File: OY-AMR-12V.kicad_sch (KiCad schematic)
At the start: 21 parts

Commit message: Upgraded to Kicad 9
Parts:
- D?: value SA16CA -> SA16CA

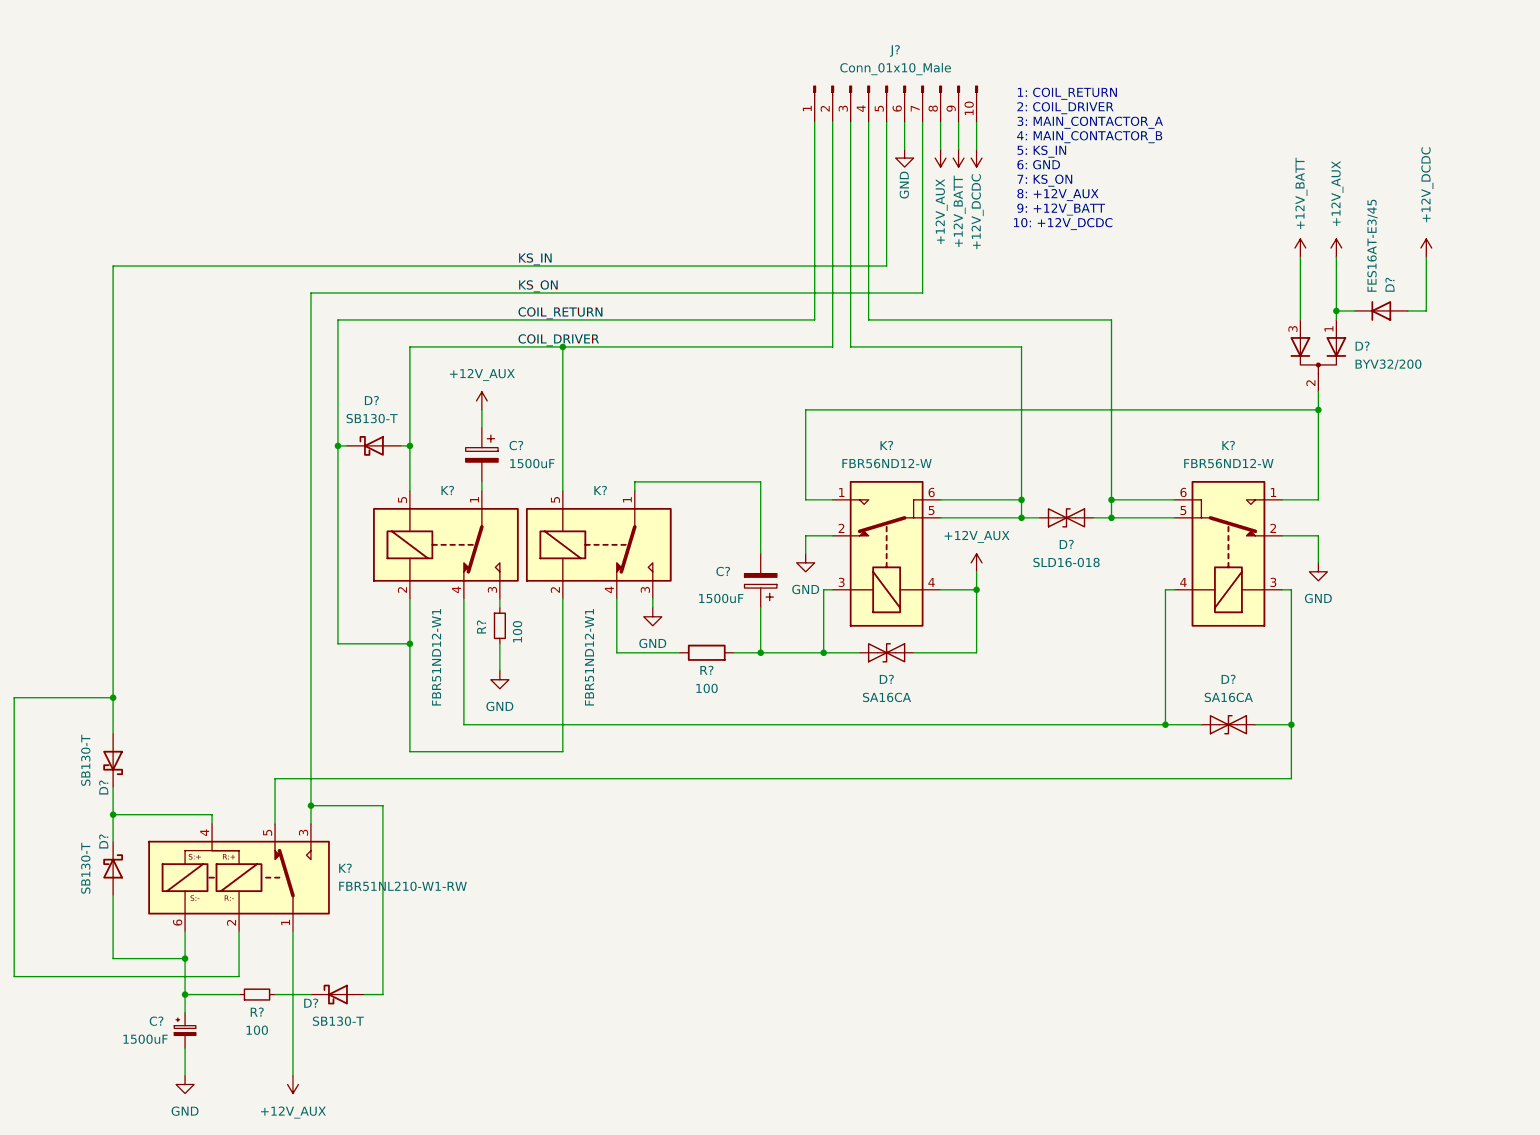
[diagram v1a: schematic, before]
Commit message: Annotated and added footprints
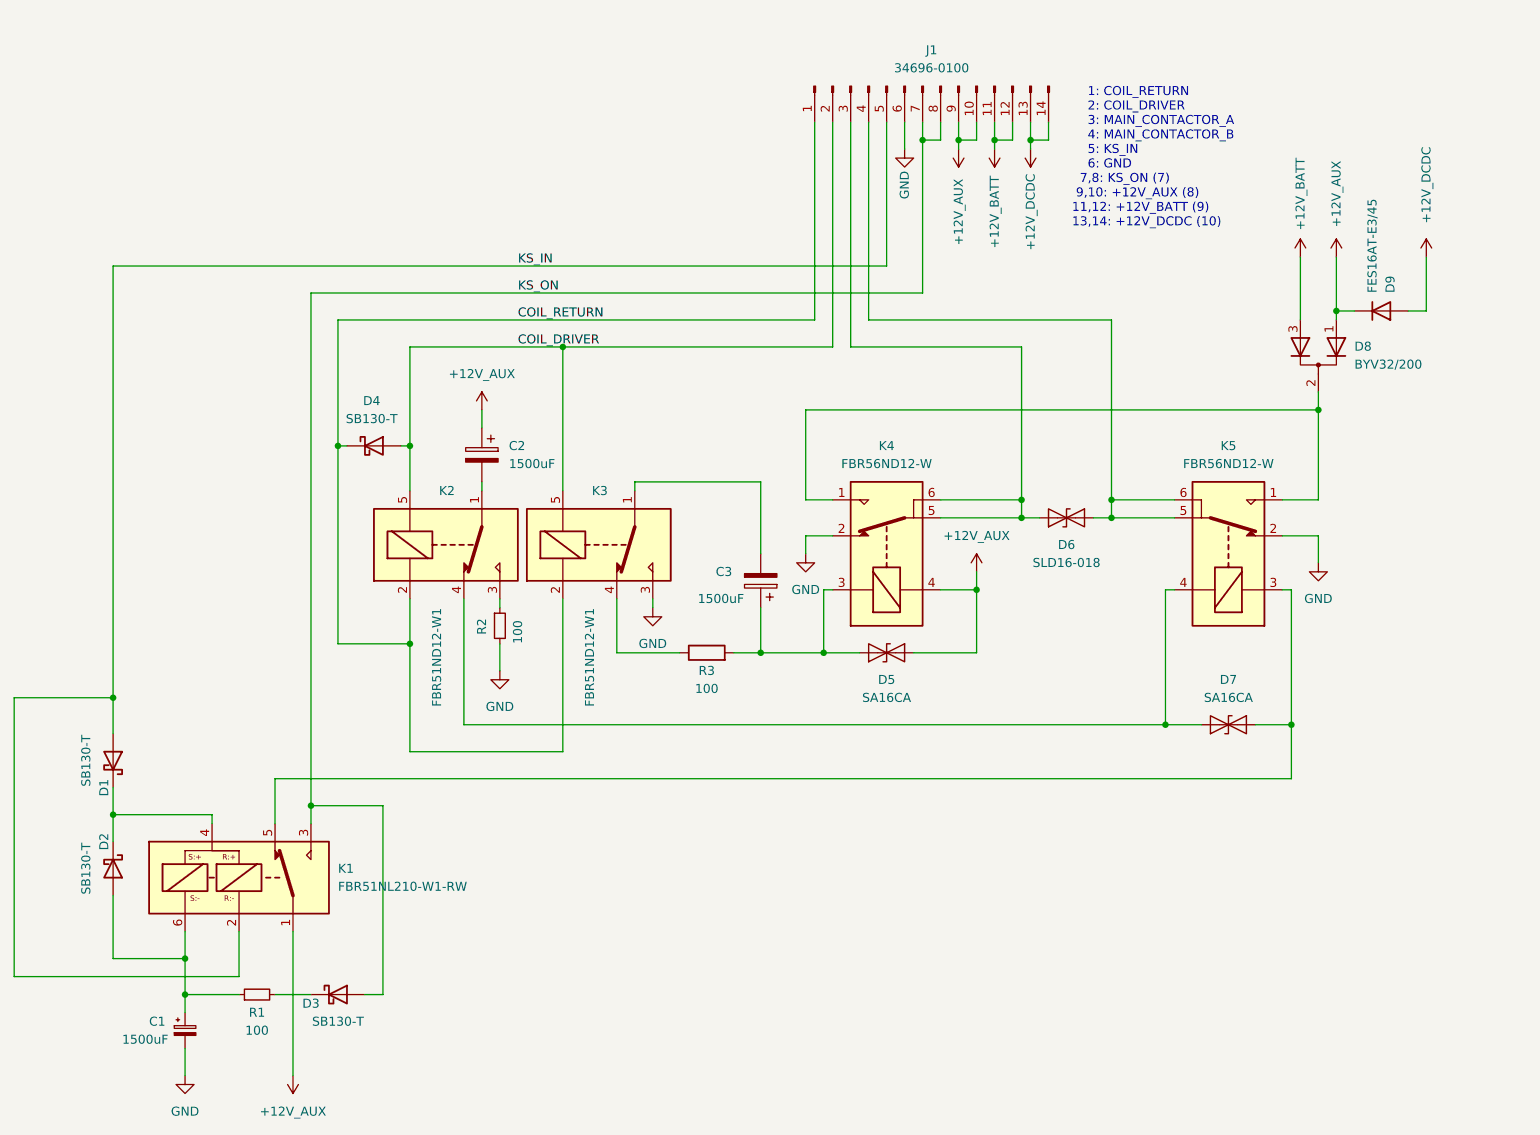
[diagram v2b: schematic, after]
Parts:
- removed J?: Conn_01x10_Male, symbol Connector:Conn_01x10_Male
- added J1: 34696-0100, SamacSys_Parts:0346960100, symbol Connector:Conn_01x14_Pin
- C1, C2, C3: renamed from C?; footprint (none) -> Capacitor_THT:CP_Radial_D16.0mm_P7.50mm
- D1, D2, D3, D4: renamed from D?; footprint (none) -> Diode_THT:D_DO-41_SOD81_P10.16mm_Horizontal
- D5, D7: renamed from D?; footprint Diode_SMD:D_SOD-323 -> Diode_THT:D_T-1_P10.16mm_Horizontal
- D6: renamed from D?; footprint (none) -> Diode_THT:D_P600_R-6_P20.00mm_Horizontal
- D8: renamed from D?; footprint (none) -> Package_TO_SOT_THT:TO-220-3_Vertical
- D9: renamed from D?; footprint (none) -> Package_TO_SOT_THT:TO-220-2_Vertical
- K1: renamed from K?; footprint (none) -> SamacSys_Parts:FBR51NL210W1RW
- K2, K3: renamed from K?; footprint Relay_THT:Relay_SPDT_Omron_G6E -> SamacSys_Parts:FBR51ND12-W1
- K4, K5: renamed from K?; footprint Relay_THT:Relay_SPDT_Omron_G6E -> SamacSys_Parts:FBR56ND12W
- R1, R2, R3: renamed from R?; footprint (none) -> Resistor_THT:R_Axial_DIN0207_L6.3mm_D2.5mm_P10.16mm_Horizontal
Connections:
- net +12V_AUX: now also J1.10 (Pin_10), J1.9 (Pin_9)
- net +12V_BATT: now also J1.11 (Pin_11), J1.12 (Pin_12)
- net +12V_DCDC: now also J1.13 (Pin_13), J1.14 (Pin_14)
- net COIL_DRIVER: now also J1.2 (Pin_2)
- net COIL_RETURN: now also J1.1 (Pin_1)
- net GND: now also J1.6 (Pin_6)
- net KS_IN: now also J1.5 (Pin_5)
- net KS_ON: now also J1.7 (Pin_7), J1.8 (Pin_8)
- net at D6.1 (A1), K4.5, K4.6: now also J1.3 (Pin_3)
- net at D6.2 (A2), K5.5, K5.6: now also J1.4 (Pin_4)
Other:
- note added: "1: COIL_RETURN 2: COIL_DRIVER 3: MAIN_CONTACTOR_A 4: MAIN_CONTACTOR_B 5: KS_IN 6: GND 7,8: KS_ON (7) 9,10: +12V_AUX (8) 11,12: +12V_BATT (9) 13,14: +12V_DCDC (10)"
- note removed: "1: COIL_RETURN 2: COIL_DRIVER 3: MAIN_CONTACTOR_A 4: MAIN_CONTACTOR_B 5: KS_IN 6: GND 7: KS_ON 8: +12V_AUX 9: +12V_BATT 10: +12V_DCDC"

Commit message: Initial PCB placements
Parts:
- D8: footprint Package_TO_SOT_THT:TO-220-3_Vertical -> Package_TO_SOT_THT:TO-220-3_Horizontal_TabDown
- D9: footprint Package_TO_SOT_THT:TO-220-2_Vertical -> Package_TO_SOT_THT:TO-220-2_Horizontal_TabDown
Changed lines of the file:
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@@
 			)
 		)
-		(property "Footprint" "Package_TO_SOT_THT:TO-220-2_Vertical"
+		(property "Footprint" "Package_TO_SOT_THT:TO-220-2_Horizontal_TabDown"
 			(at 240.03 62.23 0)
 			(effects
@@
 		(on_board yes)
 		(dnp no)
-		(fields_autoplaced yes)
 		(property "Reference" "D8"
-			(at 236.22 67.2464 90)
+			(at 222.504 66.294 90)
 			(effects
 				(font
@@
 		)
 		(property "Value" "BYV32/200"
-			(at 236.22 69.7864 90)
+			(at 215.646 68.834 90)
 			(effects
 				(font
@@
 			)
 		)
-		(property "Footprint" "Package_TO_SOT_THT:TO-220-3_Vertical"
+		(property "Footprint" "Package_TO_SOT_THT:TO-220-3_Horizontal_TabDown"
 			(at 231.14 69.85 0)
 			(effects

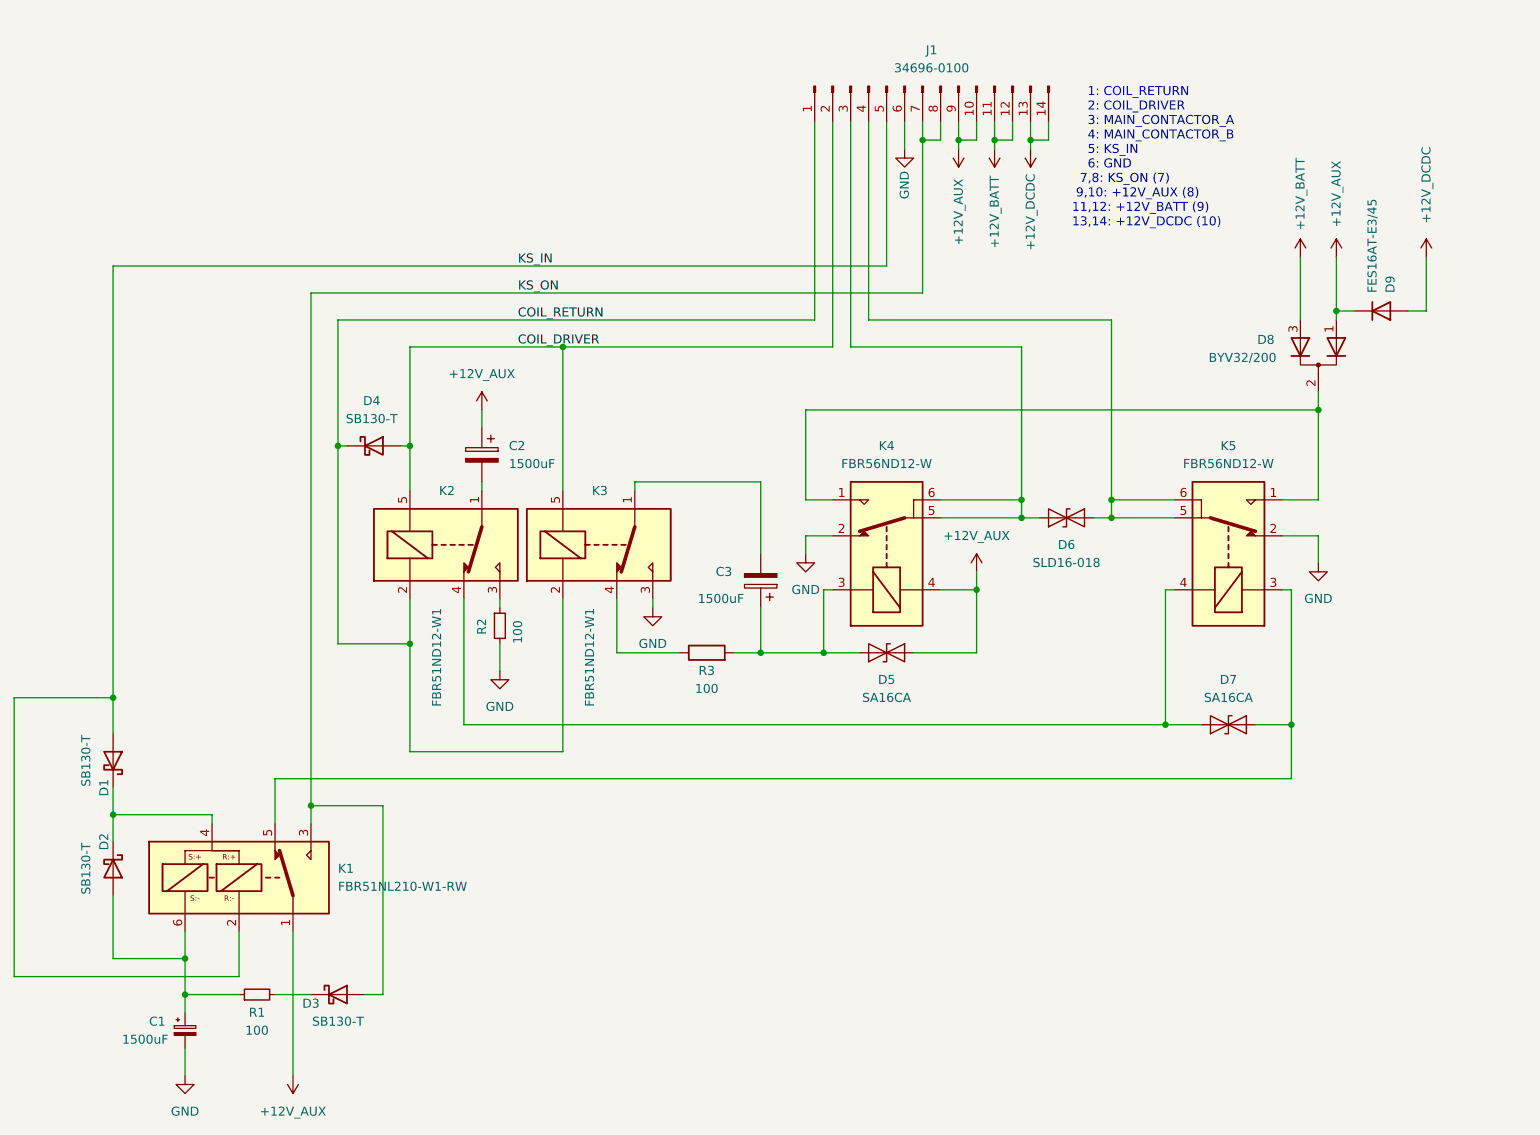
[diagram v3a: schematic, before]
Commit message: Added charge relay + precharge resistor for DC/DC
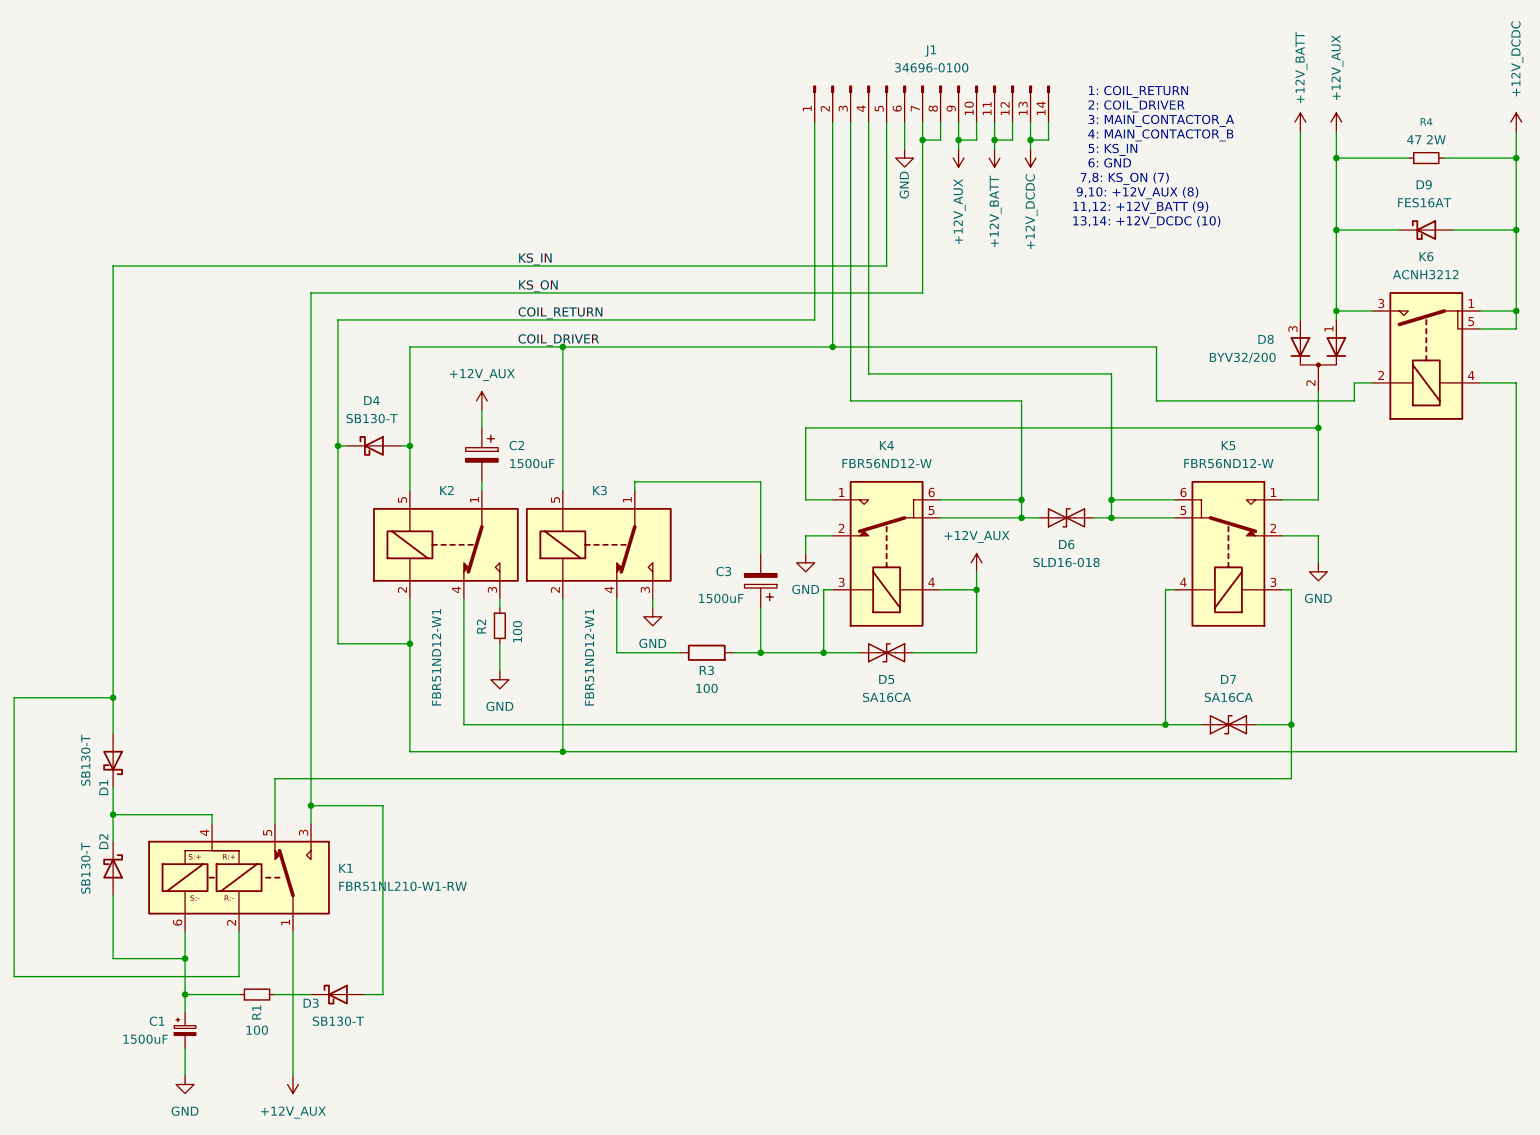
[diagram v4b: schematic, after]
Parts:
- removed D9: FES16AT-E3/45, Package_TO_SOT_THT:TO-220-2_Horizontal_TabDown, symbol Device:D
- added D9: FES16AT, Package_TO_SOT_THT:TO-220-2_Horizontal_TabDown, symbol Device:D_Schottky
- added K6: ACNH3212, SamacSys_Parts:ACNH3212, symbol Miscellaneous:ACNH3212
- added R4: 47 2W, Resistor_THT:R_Axial_DIN0411_L9.9mm_D3.6mm_P15.24mm_Horizontal, symbol Device:R_Small
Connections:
- net +12V_AUX: now also D9.1 (K), K6.3, R4.1
- net +12V_DCDC: now also D9.2 (A), K6.1, K6.5, R4.2
- net COIL_DRIVER: now also K6.2
- net COIL_RETURN: now also K6.4

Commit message: PCB layout in progress
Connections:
- net COIL_DRIVER: now also J1.6 (Pin_6); no longer J1.2 (Pin_2)
- net COIL_RETURN: now also J1.5 (Pin_5); no longer J1.1 (Pin_1)
- net GND: now also J1.2 (Pin_2); no longer J1.6 (Pin_6)
- net KS_IN: now also J1.1 (Pin_1); no longer J1.5 (Pin_5)
- net at D6.1 (A1), K4.5, K4.6: now also J1.4 (Pin_4); no longer J1.3 (Pin_3)
- net at D6.2 (A2), K5.5, K5.6: now also J1.3 (Pin_3); no longer J1.4 (Pin_4)
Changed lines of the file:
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@@
+	)
+	(junction
+		(at 172.72 67.31)
+		(diameter 0)
+		(color 0 0 0 0)
 	)
 	(junction
@@
 	)
 	(junction
-		(at 162.56 67.31)
-		(diameter 0)
-		(color 0 0 0 0)
-	)
-	(junction
 		(at 227.33 120.65)
 		(diameter 0)
@@
 	(wire
 		(pts
-			(xy 165.1 74.93) (xy 165.1 35.56)
-		)
-		(stroke
-			(width 0)
-			(type default)
-		)
-	)
-	(wire
-		(pts
 			(xy 161.29 110.49) (xy 152.4 110.49)
 		)
@@
 	(wire
 		(pts
+			(xy 167.64 35.56) (xy 167.64 74.93)
+		)
+		(stroke
+			(width 0)
+			(type default)
+		)
+	)
+	(wire
+		(pts
 			(xy 185.42 38.1) (xy 185.42 39.37)
 		)
@@
 	(wire
 		(pts
+			(xy 172.72 35.56) (xy 172.72 67.31)
+		)
+		(stroke
+			(width 0)
+			(type default)
+		)
+	)
+	(wire
+		(pts
 			(xy 233.68 50.8) (xy 242.57 50.8)
 		)
@@
 	(wire
 		(pts
-			(xy 162.56 67.31) (xy 162.56 35.56)
-		)
-		(stroke
-			(width 0)
-			(type default)
-		)
-	)
-	(wire
-		(pts
-			(xy 189.23 74.93) (xy 165.1 74.93)
+			(xy 189.23 74.93) (xy 167.64 74.93)
 		)
 		(stroke
@@
 	(wire
 		(pts
-			(xy 60.96 55.88) (xy 170.18 55.88)
+			(xy 60.96 55.88) (xy 160.02 55.88)
 		)
 		(stroke
@@
 	(wire
 		(pts
+			(xy 172.72 67.31) (xy 208.28 67.31)
+		)
+		(stroke
+			(width 0)
+			(type default)
+		)
+	)
+	(wire
+		(pts
 			(xy 102.87 109.22) (xy 92.71 109.22)
 		)
@@
 	(wire
 		(pts
-			(xy 172.72 35.56) (xy 172.72 39.37)
+			(xy 162.56 35.56) (xy 162.56 39.37)
 		)
 		(stroke
@@
 	(wire
 		(pts
-			(xy 124.46 67.31) (xy 162.56 67.31)
-		)
-		(stroke
-			(width 0)
-			(type default)
-		)
-	)
-	(wire
-		(pts
 			(xy 60.96 55.88) (xy 60.96 116.84)
 		)
@@
 	(wire
 		(pts
-			(xy 201.93 71.12) (xy 167.64 71.12)
-		)
-		(stroke
-			(width 0)
-			(type default)
-		)
-	)
-	(wire
-		(pts
 			(xy 158.75 96.52) (xy 158.75 93.98)
 		)
@@
 	(wire
 		(pts
-			(xy 162.56 67.31) (xy 208.28 67.31)
+			(xy 124.46 67.31) (xy 172.72 67.31)
 		)
 		(stroke
@@
 	(wire
 		(pts
-			(xy 170.18 55.88) (xy 170.18 35.56)
-		)
-		(stroke
-			(width 0)
-			(type default)
-		)
-	)
-	(wire
-		(pts
-			(xy 92.71 63.5) (xy 160.02 63.5)
+			(xy 92.71 63.5) (xy 170.18 63.5)
 		)
 		(stroke
@@
 	(wire
 		(pts
-			(xy 160.02 63.5) (xy 160.02 35.56)
+			(xy 170.18 63.5) (xy 170.18 35.56)
 		)
 		(stroke
@@
 	(wire
 		(pts
+			(xy 160.02 55.88) (xy 160.02 35.56)
+		)
+		(stroke
+			(width 0)
+			(type default)
+		)
+	)
+	(wire
+		(pts
 			(xy 162.56 101.6) (xy 161.29 101.6)
 		)
@@
 	(wire
 		(pts
+			(xy 165.1 71.12) (xy 201.93 71.12)
+		)
+		(stroke
+			(width 0)
+			(type default)
+		)
+	)
+	(wire
+		(pts
 			(xy 152.4 86.36) (xy 152.4 96.52)
 		)
@@
 	(wire
 		(pts
-			(xy 167.64 71.12) (xy 167.64 35.56)
-		)
-		(stroke
-			(width 0)
-			(type default)
-		)
-	)
-	(wire
-		(pts
 			(xy 177.8 91.44) (xy 189.23 91.44)
 		)
@@
 		(pts
 			(xy 201.93 88.9) (xy 201.93 71.12)
+		)
+		(stroke
+			(width 0)
+			(type default)
+		)
+	)
+	(wire
+		(pts
+			(xy 165.1 35.56) (xy 165.1 71.12)
 		)
 		(stroke
@@
 	(symbol
 		(lib_id "power:GND")
-		(at 172.72 39.37 0)
+		(at 162.56 39.37 0)
 		(unit 1)
 		(exclude_from_sim no)
@@
 		(dnp no)
 		(property "Reference" "#PWR0115"
-			(at 172.72 45.72 0)
+			(at 162.56 45.72 0)
 			(effects
 				(font
@@
 		)
 		(property "Value" "GND"
-			(at 172.72 44.45 90)
+			(at 162.56 44.45 90)
 			(effects
 				(font
@@
 		)
 		(property "Footprint" ""
-			(at 172.72 39.37 0)
+			(at 162.56 39.37 0)
 			(effects
 				(font
@@
 		)
 		(property "Datasheet" ""
-			(at 172.72 39.37 0)
+			(at 162.56 39.37 0)
 			(effects
 				(font
@@
 		)
 		(property "Description" ""
-			(at 172.72 39.37 0)
-			(effects
-				(font
+			(at 162.56 39.37 0)
+			(effects
+				(font

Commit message: PCB layout v0.1 ready for prototype production
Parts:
- D8: footprint Package_TO_SOT_THT:TO-220-3_Horizontal_TabDown -> Package_TO_SOT_THT:TO-220-3_Vertical
- D9: footprint Package_TO_SOT_THT:TO-220-2_Horizontal_TabDown -> Package_TO_SOT_THT:TO-220-2_Vertical
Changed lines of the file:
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@@
 			)
 		)
-		(property "Footprint" "Package_TO_SOT_THT:TO-220-2_Horizontal_TabDown"
+		(property "Footprint" "Package_TO_SOT_THT:TO-220-2_Vertical"
 			(at 246.38 50.8 0)
 			(effects
@@
 		(dnp no)
 		(property "Reference" "D8"
-			(at 222.504 66.294 90)
+			(at 236.982 65.786 90)
 			(effects
 				(font
@@
 		)
 		(property "Value" "BYV32/200"
-			(at 215.646 68.834 90)
+			(at 236.728 69.088 90)
 			(effects
 				(font
@@
 			)
 		)
-		(property "Footprint" "Package_TO_SOT_THT:TO-220-3_Horizontal_TabDown"
+		(property "Footprint" "Package_TO_SOT_THT:TO-220-3_Vertical"
 			(at 231.14 69.85 0)
 			(effects
